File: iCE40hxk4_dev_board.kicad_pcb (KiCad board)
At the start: 4 copper layers, 70 x 152 mm, 339 parts, among them J101 CONN_01X01, J1101 CONN_01X25, J201 CONN_01X02, J202 USB_OTG, J701 CONN_01X01, J702 CONN_01X01, SW1101 SW_Push, U1001 ADC1175, U1002 ADC1175, U1101 MIC7300, U1102 MIC7300, U1103 MCP4716, U1104 MCP4716, U1105 MIC7300, U1106 MIC7300, U201 MIC2005A-2YM5, U203 93LCxxB_sot-23-6, U204 MIC5355/6-xYMME, U205 FT2232H, U301 iCE40-HX4K-TQ144, U302 25LC_EEPROM, U501 AS4C1M16S, U701 CPC1017N, U702 CPC1017N, U703 CD4051BM96, U704 CD4051BM96, U801 CD4051BM96, U802 CD4051BM96, U803 CLC4007, U901 LM2776DBVR, U902 TCR2EF13, U903 MIC5270

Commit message: Doing re-routing
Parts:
- removed D205: GREEN, LEDs:LED_0603
- removed D206: YELLOW, LEDs:LED_0603
- removed D207: RED, LEDs:LED_0603
- removed J201: CONN_01X02, Pin_Headers:Pin_Header_Angled_1x02_Pitch1.27mm
- removed J702: CONN_01X01, Pin_Headers:Pin_Header_Straight_1x01_Pitch1.27mm
- removed R232, R233, R234: 680, Resistors_SMD:R_0603_HandSoldering
- added J1001, J1002, J1003, J1004, J405, J406, J501, J502, J603, J604, J605, J703, J704, J705, J706, J801, J802, J803, J804, J805, J806, J807, J808, J809, J810: Testpoint, library:Via-0.8mm, F.Cu at (118.9, 200.8)
- added J1005: USB_EXT, Connectors:USB_Micro-B, F.Cu at (147.4, 163.7)
- added J102: NRJ6HM-1, library:NRJ6HM-1_audio_jack, F.Cu at (119.5, 36.7)
- added J103: CONN_COAXIAL, library:Molex_73100-0105_BNC, F.Cu at (139.9, 34.4)
- added J104: CONN_COAXIAL, library:Molex_73100-0105_BNC, F.Cu at (98.9, 34.4)
- added J401: Testpoint, library:Via-0.8mm, F.Cu at (136.1, 68.6)
- added J402: Testpoint, library:Via-0.8mm, F.Cu at (136.1, 70.4)
- added J404: Testpoint, library:Via-0.8mm, F.Cu at (92.3, 52.0)
- added J601: CONN_01X02, Pin_Headers:Pin_Header_Straight_1x02_Pitch1.27mm, F.Cu at (115.0, 66.8)
- added J602: CONN_01X02, Pin_Headers:Pin_Header_Straight_1x02_Pitch1.27mm, F.Cu at (136.4, 66.8)
- C1101, C1102, C905: value 0.1uF -> 100nF
- C205: value 4.7u -> 4.7uF; footprint Capacitors_SMD:CP_Elec_5x5.3 -> Capacitors_SMD:C_1206_HandSoldering
- C207: value 4.7u -> 4.7uF; footprint Capacitors_SMD:CP_Elec_5x5.7 -> Capacitors_SMD:C_1206_HandSoldering
- C213, C215: value 4.7u -> 4.7uF
- C701, C702: value 100p -> 100pF
- C703, C706: value 22p -> 22pF
- C704, C707: value 0.56-3.58p -> 1-3pF; footprint Capacitors_SMD:C_0603_HandSoldering -> Capacitors_THT:CP_Radial_Tantal_D6.0mm_P5.00mm
- C705, C708: footprint Capacitors_SMD:C_0603_HandSoldering -> Capacitors_THT:CP_Radial_Tantal_D6.0mm_P5.00mm
- C713, C714: value Optional -> Not used; footprint Capacitors_SMD:C_0603_HandSoldering -> Capacitors_THT:CP_Radial_Tantal_D6.0mm_P5.00mm
- C901, C902: footprint Capacitors_SMD:C_0805_HandSoldering -> Capacitors_SMD:C_0603_HandSoldering
- D201, D208: value D_Schottky -> D_Schottky_CDBURT0530LL-HF
- D202: value LED_ALT -> GREEN
- D301: value D -> D_BAS21,215
- J101: value CONN_01X01 -> CONN_01X02; footprint Pin_Headers:Pin_Header_Angled_1x01_Pitch1.27mm -> Pin_Headers:Pin_Header_Straight_1x02_Pitch1.27mm
- J701: value CONN_01X01 -> Testpoint; footprint Pin_Headers:Pin_Header_Straight_1x01_Pitch1.27mm -> library:Via-0.8mm
- L1001, L1002, L1003, L1004, L1005, L1006, L1007: value L_Core_Iron_Small -> L_BLM18AG121SN1D; footprint Capacitors_SMD:C_0603_HandSoldering -> Inductors_SMD:L_0603_HandSoldering
- L201, L202: value BK0603HS330-T -> L_BLM18BA750SZ1D
- L203, L204: value BLM18BA750SZ1D -> L_BLM18BA750SZ1D
- R1001, R1004: value 50 -> 50R
- R1002, R1005, R1103, R1104, R213, R214, R215, R216, R217, R218, R219, R220, R221, R222, R223, R224, R225, R226, R227, R228, R229, R230, R231, R709, R710, R801, R803: value 0 -> 0R
- R1003, R1012, R1013, R811, R812, R815, R817, R818, R820: value 220 -> 220R
- R101, R1105, R1106, R1107, R1108, R1109, R1110, R207, R209, R210, R301, R302, R303, R304, R305, R306, R704, R708: value 10k -> 10K
- R1010, R1011, R805, R806, R807, R808: value 470 -> 470R
- R1101, R1102, R802, R804: value 1G -> Let it open
- R1111, R1112: value 330 -> 330R
- R1114, R1117: value 1k2 -> 1K2
- R201: value 100k -> 10K
- R202, R204, R205: value 1500 -> 1K5
- R208: value 2k2 -> 2K2
- R211: value 12k -> 12K
- R212: value 1k -> 1K
- R307, R308, R821, R823, R824, R826: value 100 -> 100R
- R401, R402, R403, R404, R405, R406, R407, R408: value 680 -> 680R
- R701, R705: value 13k -> 13K
- R702, R706: value 887k -> 887K
- R703, R707: value 89.8k -> 89K8
- R833, R834, R835, R836, R837, R838, R839, R840: value R -> Not used
- U203: value 93LCxxB_sot-23-6 -> 93LC56BT-I/O
- moved J701 135.3 mm to (118.9, 200.8)
- moved C713 31.9 mm to (158.2, 63.3)
- moved C707 26.4 mm to (156.6, 56.5)
- moved C708 26.2 mm to (157.3, 47.2)
- moved C714 16.3 mm to (99.5, 44.7), turned to 180 degrees
- moved C705 13.9 mm to (99.5, 58.9), turned to 180 degrees
- moved C703 12.9 mm to (102.1, 49.1), turned to 270 degrees
- moved C704 12.8 mm to (99.5, 51.9), turned to 180 degrees
- moved C710 11.3 mm to (102.1, 61.6), turned to 270 degrees
- moved C709 11.2 mm to (102.1, 53.1), turned to 270 degrees
- moved R704 10.2 mm to (103.9, 61.7), turned to 270 degrees
- moved R710 7.46 mm to (102.1, 57.5), turned to 270 degrees
- moved SW1101 6.94 mm to (141.9, 68.4)
- moved R701 5.99 mm to (103.9, 49.2), turned to 270 degrees
- moved C701 5.21 mm to (104.8, 46.3), turned to 0 degrees
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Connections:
- net /Analog front end/CHA_INPUT_SIGNAL renamed /CHA
- net /Analog front end/CHB_INPUT_SIGNAL renamed /CHB
- J101 pad 1: Net-(J101-Pad1) -> GND
- J701 pad 1: Net-(J701-Pad1) -> /Analog front end/ADC/CHB_V_REF_TOP
- R101 pad 2: Net-(J101-Pad1) -> Net-(J101-Pad2)
- U703 pad 15: Net-(J701-Pad1) -> Net-(J601-Pad2)
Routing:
- net GND: track 1450.0 -> 1519.0 mm, vias 202 -> 196
- net /CHB: track 2.77 -> 42.2 mm, vias 0 -> 1
- net /CHA: track 3.35 -> 38.8 mm
- net /Analog front end/CHA_DC_COUPLING: track 154.3 -> 120.3 mm
- net /Analog front end/ATTENUATION/CHA_ATT_40dB: track 14.5 -> 40.9 mm, vias 0 -> 1
- net /Analog front end/+3V3_A: track 306.7 -> 291.4 mm, vias 16 -> 15
- net /Analog front end/-3V0: track 208.0 -> 193.5 mm, vias 12 -> 11
- net Net-(C701-Pad1): track 17.2 -> 8.67 mm
- net (no net): track 0.00 -> 6.10 mm
- net Net-(SW1101-Pad1): track 95.8 -> 89.9 mm
- net Net-(C202-Pad1): track 6.99 -> 11.2 mm
- net /Analog front end/ATTENUATION/CHB_ATT_20dB: track 23.0 -> 26.8 mm
- net /Analog front end/ATTENUATION/CHB_ATT_40dB: track 15.3 -> 19.1 mm
- net Net-(J101-Pad2): track 0.00 -> 3.18 mm
- net Net-(J101-Pad1): track 3.18 -> 0.00 mm
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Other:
- board size 70 x 152 mm -> 66.4 x 162.5 mm

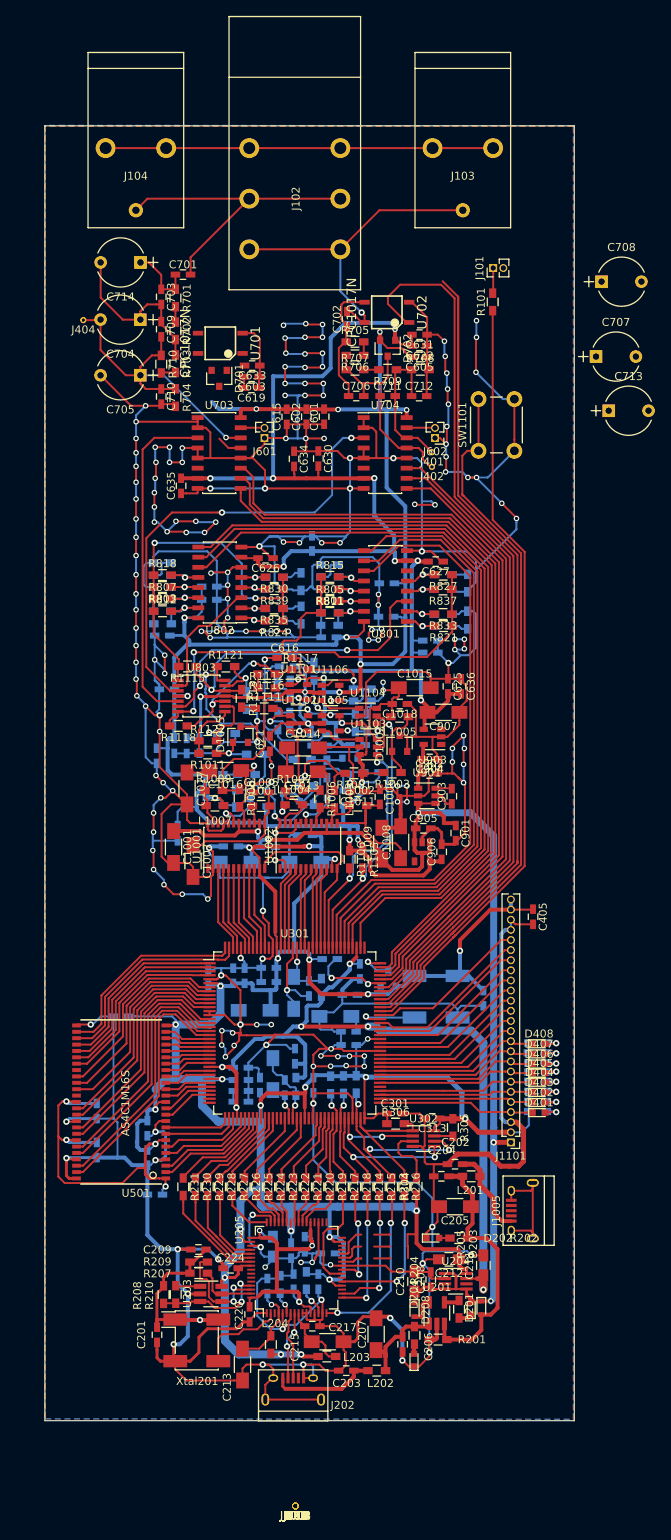
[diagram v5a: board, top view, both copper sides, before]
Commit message: Rerouted with trimmer caps corrected footprints
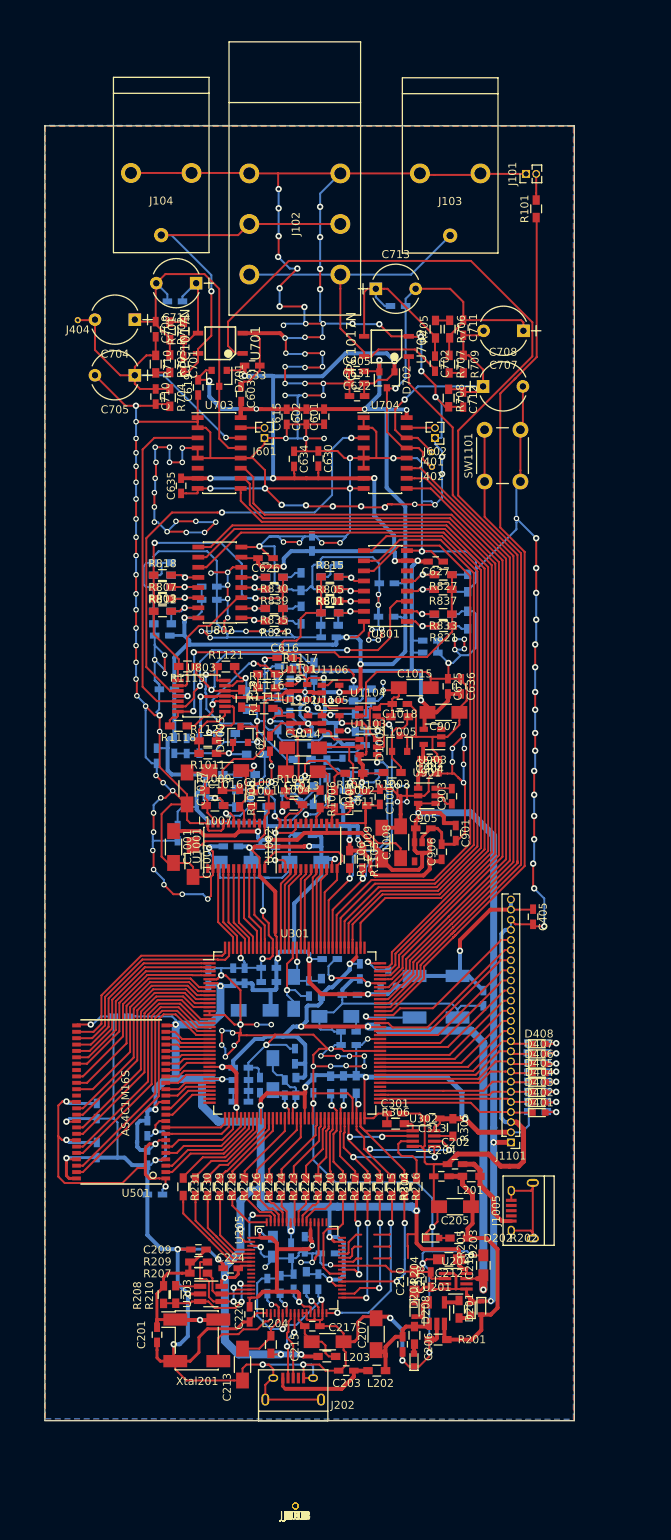
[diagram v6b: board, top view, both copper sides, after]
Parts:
- C703, C706: moved to B.Cu
- moved C713 33.0 mm to (129.0, 48.0)
- moved C708 19.9 mm to (142.5, 60.3)
- moved R101 12.9 mm to (149.1, 38.0)
- moved C711 12.8 mm to (140.0, 52.9), turned to 270 degrees
- moved J101 12.5 mm to (147.9, 33.6)
- moved C706 12.5 mm to (131.8, 50.2)
- moved C702 12.4 mm to (136.4, 57.4), turned to 270 degrees
- moved R706 12.3 mm to (138.3, 53.1), turned to 270 degrees
- moved R707 11.8 mm to (138.2, 57.5), turned to 270 degrees
- moved C701 11.2 mm to (104.9, 57.5), turned to 270 degrees
- moved R705 10.2 mm to (136.5, 53.1), turned to 90 degrees
- moved C622 10.1 mm to (126.7, 61.5), turned to 0 degrees
- moved C631 9.99 mm to (126.6, 59.9), turned to 0 degrees
- moved C707 9.67 mm to (147.5, 53.3), turned to 180 degrees
- moved R709 9.52 mm to (140.0, 57.5), turned to 270 degrees
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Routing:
- net GND: track 1519.0 -> 1645.2 mm, vias 196 -> 222
- net /Analog front end/CHA_DC_COUPLING: track 120.3 -> 150.3 mm
- net /Analog front end/ATTENUATION/CHB_ATT_20dB: track 26.8 -> 51.0 mm, vias 0 -> 1
- net /Analog front end/ATTENUATION/CHA_ATT_20dB: track 24.9 -> 46.6 mm
- net /Analog front end/CHB_DC_COUPLING: track 112.8 -> 93.6 mm
- net /Analog front end/ATTENUATION/CHB_ATT_40dB: track 19.1 -> 36.0 mm, vias 0 -> 1
- net /RIGHT_TOP_BANKs/IOT_146: track 98.3 -> 111.8 mm
- net /CHB: track 42.2 -> 49.3 mm, vias 1 -> 0
- net Net-(SW1101-Pad1): track 89.9 -> 83.0 mm
- net /CHA: track 38.8 -> 45.4 mm, vias 0 -> 1
- net /Analog front end/-3V0: track 193.5 -> 199.1 mm, vias 11 -> 12
- net Net-(C701-Pad1): track 8.67 -> 13.8 mm
- net Net-(C702-Pad1): track 18.3 -> 23.0 mm
- net /Analog front end/+3V3_A: track 291.4 -> 292.8 mm, vias 15 -> 16
- net /Analog front end/ATTENUATION/CHA_ATT_40dB: track 40.9 -> 41.6 mm
